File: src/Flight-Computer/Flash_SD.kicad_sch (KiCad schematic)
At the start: 7 parts

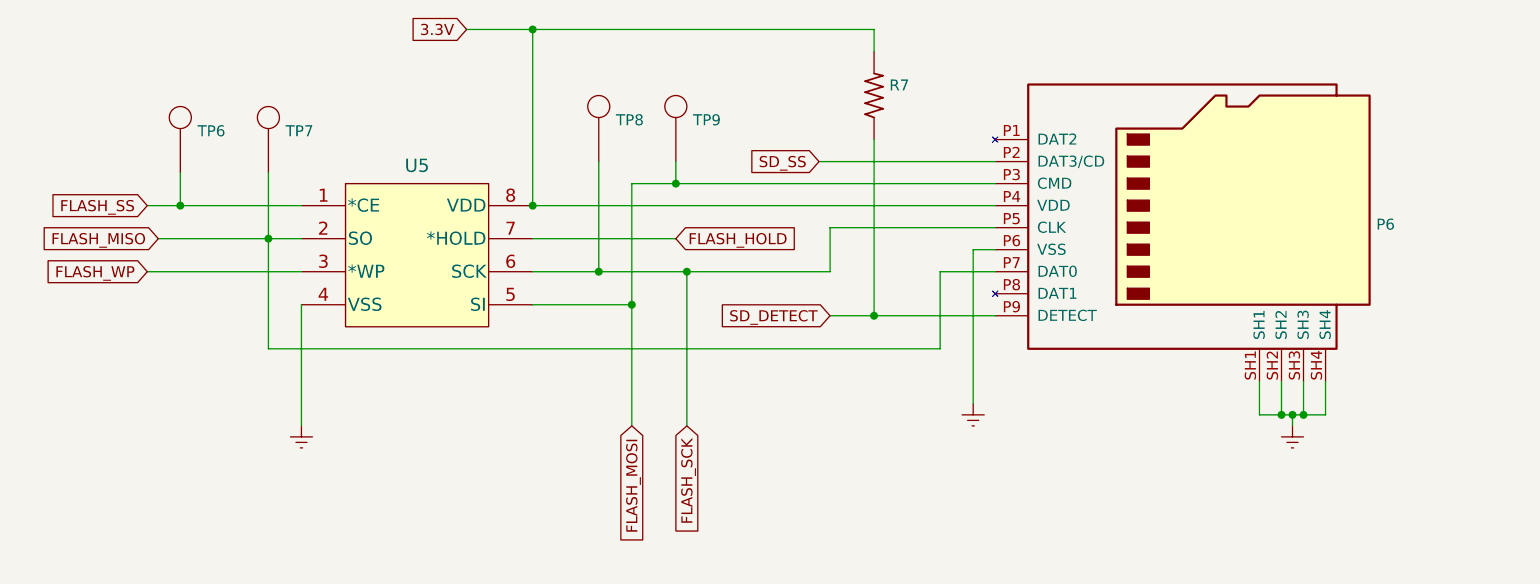
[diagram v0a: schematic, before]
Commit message: implemented crystal oscillator in schematic
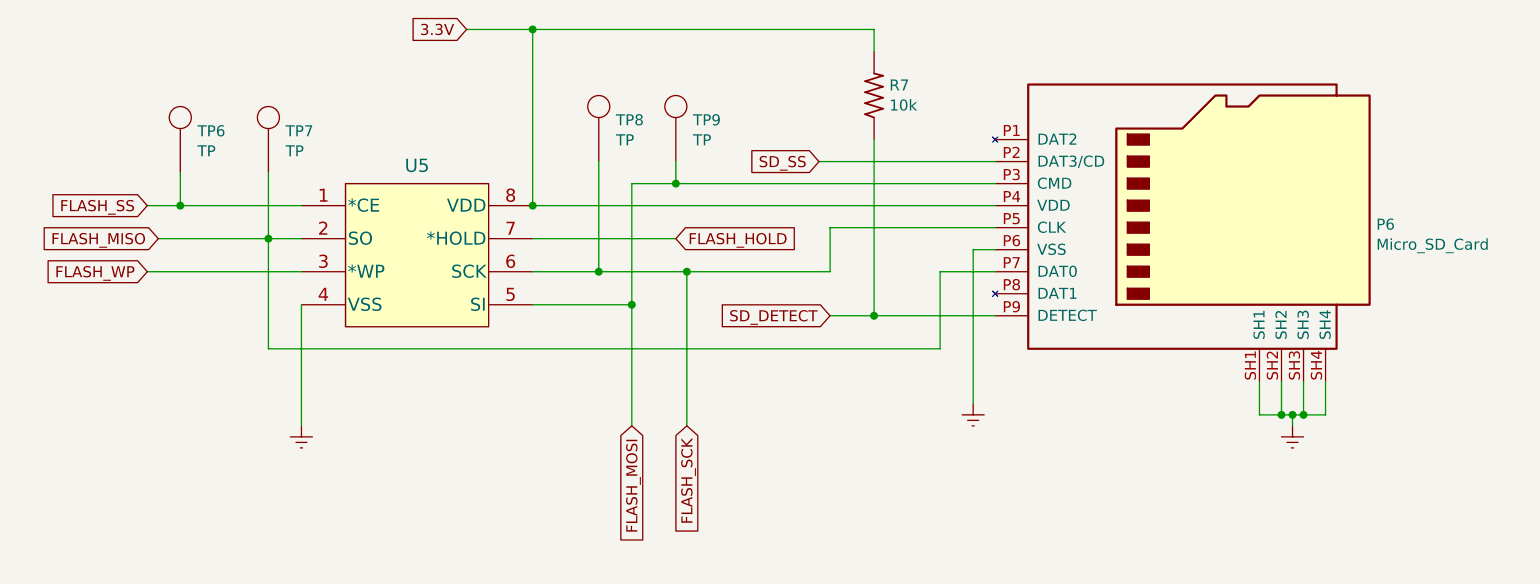
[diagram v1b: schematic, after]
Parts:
- P6: value (none) -> Micro_SD_Card; footprint (none) -> Engine-Controller:GCT_MEM2075-00-140-01-A
- R7: value (none) -> 10k; footprint (none) -> Engine-Controller:RES_0603
- TP6, TP7, TP8, TP9: value (none) -> TP; footprint (none) -> Engine-Controller:TP
- U5: value (none) -> SST25VF040B-50-4I-S2AE-T; footprint (none) -> Engine-Controller:SST25VF040B-50-4I-S2AE-T
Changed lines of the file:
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@@
       (effects (font (size 1.524 1.524)))
     )
-    (property "Value" "" (id 1) (at 114.935 91.9226 0)
+    (property "Value" "SST25VF040B-50-4I-S2AE-T" (id 1) (at 114.935 91.9226 0)
       (effects (font (size 1.524 1.524)) hide)
     )
-    (property "Footprint" "" (id 2) (at 115.57 116.84 0)
+    (property "Footprint" "Engine-Controller:SST25VF040B-50-4I-S2AE-T" (id 2) (at 115.57 116.84 0)
       (effects (font (size 1.524 1.524)) hide)
     )
@@
       (effects (font (size 1.27 1.27)) hide)
     )
-    (property "Value" "" (id 1) (at 101.6 125.73 0)
+    (property "Value" "Earth" (id 1) (at 101.6 125.73 0)
       (effects (font (size 1.27 1.27)) hide)
     )
@@
       (effects (font (size 1.27 1.27)) (justify left))
     )
-    (property "Value" "" (id 1) (at 225.552 101.0158 0)
+    (property "Value" "Micro_SD_Card" (id 1) (at 225.552 101.0158 0)
       (effects (font (size 1.27 1.27)) (justify left))
     )
-    (property "Footprint" "" (id 2) (at 233.68 88.9 0)
+    (property "Footprint" "Engine-Controller:GCT_MEM2075-00-140-01-A" (id 2) (at 233.68 88.9 0)
       (effects (font (size 1.27 1.27)) hide)
     )
@@
       (effects (font (size 1.27 1.27)) hide)
     )
-    (property "Value" "" (id 1) (at 215.9 125.73 0)
+    (property "Value" "Earth" (id 1) (at 215.9 125.73 0)
       (effects (font (size 1.27 1.27)) hide)
     )
@@
       (effects (font (size 1.27 1.27)) hide)
     )
-    (property "Value" "" (id 1) (at 179.07 123.19 0)
+    (property "Value" "Earth" (id 1) (at 179.07 123.19 0)
       (effects (font (size 1.27 1.27)) hide)
     )
@@
       (effects (font (size 1.27 1.27)) (justify right))
     )
-    (property "Value" "" (id 1) (at 169.3926 84.963 90)
+    (property "Value" "10k" (id 1) (at 169.3926 84.963 90)
       (effects (font (size 1.27 1.27)) (justify right))
     )
-    (property "Footprint" "" (id 2) (at 180.34 82.55 0)
+    (property "Footprint" "Engine-Controller:RES_0603" (id 2) (at 180.34 82.55 0)
       (effects (font (size 1.27 1.27)) (justify left bottom) hide)
     )
@@
       (effects (font (size 1.27 1.27)) (justify left))
     )
-    (property "Value" "" (id 1) (at 89.6112 90.2462 0)
+    (property "Value" "TP" (id 1) (at 89.6112 90.2462 0)
       (effects (font (size 1.27 1.27)) (justify left))
     )
-    (property "Footprint" "" (id 2) (at 87.63 92.71 0)
+    (property "Footprint" "Engine-Controller:TP" (id 2) (at 87.63 92.71 0)
       (effects (font (size 1.27 1.27)) hide)
     )
@@
       (effects (font (size 1.27 1.27)) (justify left))
     )
-    (property "Value" "" (id 1) (at 99.7712 90.2462 0)
+    (property "Value" "TP" (id 1) (at 99.7712 90.2462 0)
       (effects (font (size 1.27 1.27)) (justify left))
     )
-    (property "Footprint" "" (id 2) (at 97.79 92.71 0)
+    (property "Footprint" "Engine-Controller:TP" (id 2) (at 97.79 92.71 0)
       (effects (font (size 1.27 1.27)) hide)
     )
@@
       (effects (font (size 1.27 1.27)) (justify left))
     )
-    (property "Value" "" (id 1) (at 137.8712 88.9762 0)
+    (property "Value" "TP" (id 1) (at 137.8712 88.9762 0)
       (effects (font (size 1.27 1.27)) (justify left))
     )
-    (property "Footprint" "" (id 2) (at 135.89 91.44 0)
+    (property "Footprint" "Engine-Controller:TP" (id 2) (at 135.89 91.44 0)
       (effects (font (size 1.27 1.27)) hide)
     )
@@
       (effects (font (size 1.27 1.27)) (justify left))
     )
-    (property "Value" "" (id 1) (at 146.7612 88.9762 0)
+    (property "Value" "TP" (id 1) (at 146.7612 88.9762 0)
       (effects (font (size 1.27 1.27)) (justify left))
     )
-    (property "Footprint" "" (id 2) (at 144.78 91.44 0)
+    (property "Footprint" "Engine-Controller:TP" (id 2) (at 144.78 91.44 0)
       (effects (font (size 1.27 1.27)) hide)
     )
